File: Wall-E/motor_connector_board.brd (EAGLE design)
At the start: 104.1 x 41.9 mm, 19 parts, among them U1 JST_SH_4, U2 JST_SH_6, U3 JST_SH_6, U4 MOLEX_ULTRAFIT, U5 SMC

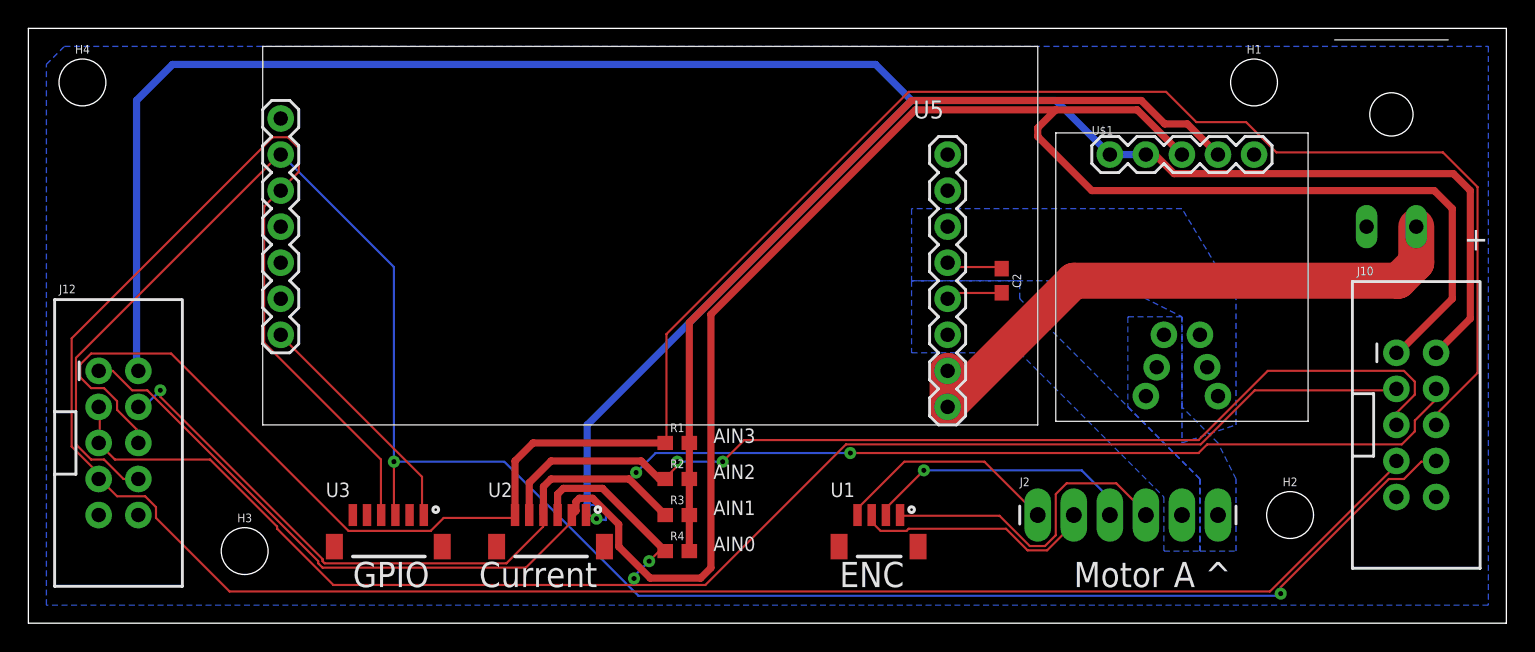
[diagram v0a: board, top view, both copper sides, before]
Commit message: completed first motor pcb
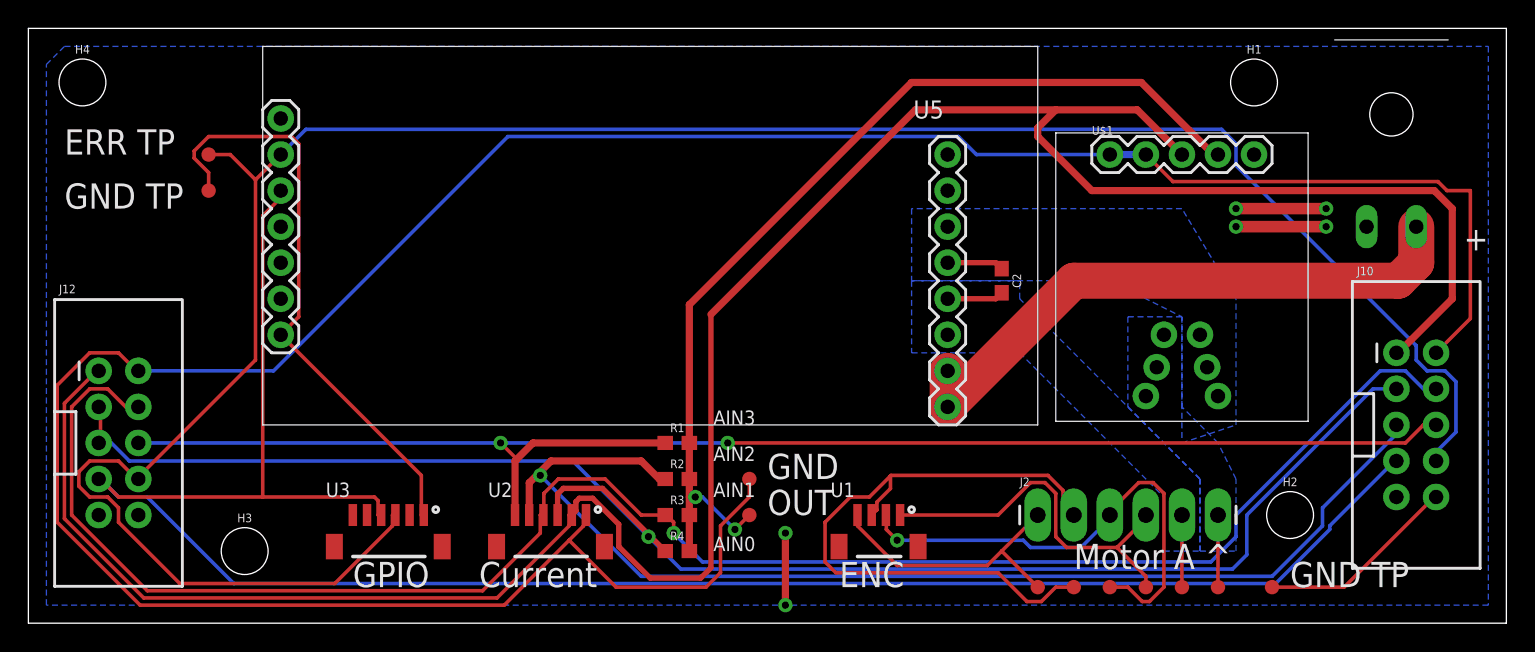
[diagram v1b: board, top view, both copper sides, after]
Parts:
- added TP1, TP10, TP11, TP2, TP3, TP4, TP5, TP6, TP7, TP8, TP9: TEST-POINT3X4, SparkFun-Connectors:PAD.03X.04
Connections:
- net ACS_GND: now also TP4.P$1
- net ACS_OUT: now also TP5.P$1
- net ENC_A: now also TP6.P$1
- net ENC_B: now also TP7.P$1
- net ENC_GND: now also TP9.P$1
- net ENC_VCC: now also TP8.P$1
- net GND: now also TP1.P$1, TP2.P$1
- net MOTORA: now also TP10.P$1
- net MOTORB: now also TP11.P$1
- net SMC_ERR: now also TP3.P$1
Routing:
- net GND: track 16.9 -> 74.1 mm, vias 0 -> 6
- net AIN3: track 152.0 -> 108.5 mm, vias 0 -> 2
- net ENC_A: track 17.1 -> 45.8 mm
- net SMC_ERR: track 142.2 -> 164.0 mm, vias 2 -> 0
- net ACS_GND: track 172.5 -> 194.2 mm, vias 1 -> 0
- net SMC_RST: track 162.4 -> 141.9 mm
- net AIN1: track 108.6 -> 126.5 mm, vias 3 -> 1
- net ENC_VCC: track 19.3 -> 34.9 mm
- net ACS_VCC: track 159.1 -> 170.5 mm
- net AIN2: track 73.1 -> 82.1 mm, vias 2 -> 1
- net ACS_OUT: track 61.4 -> 68.8 mm, vias 0 -> 2
- net MOTORA: track 0.00 -> 5.08 mm
- net MOTORB: track 4.05 -> 9.06 mm
- net ENC_GND: track 22.8 -> 26.7 mm
- net ENC_B: track 16.1 -> 19.7 mm
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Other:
- board text added: "ERR TP"
- board text added: "GND"
- board text added: "GND TP"
- board text added: "OUT"

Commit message: fixed error on ribbon cable connector
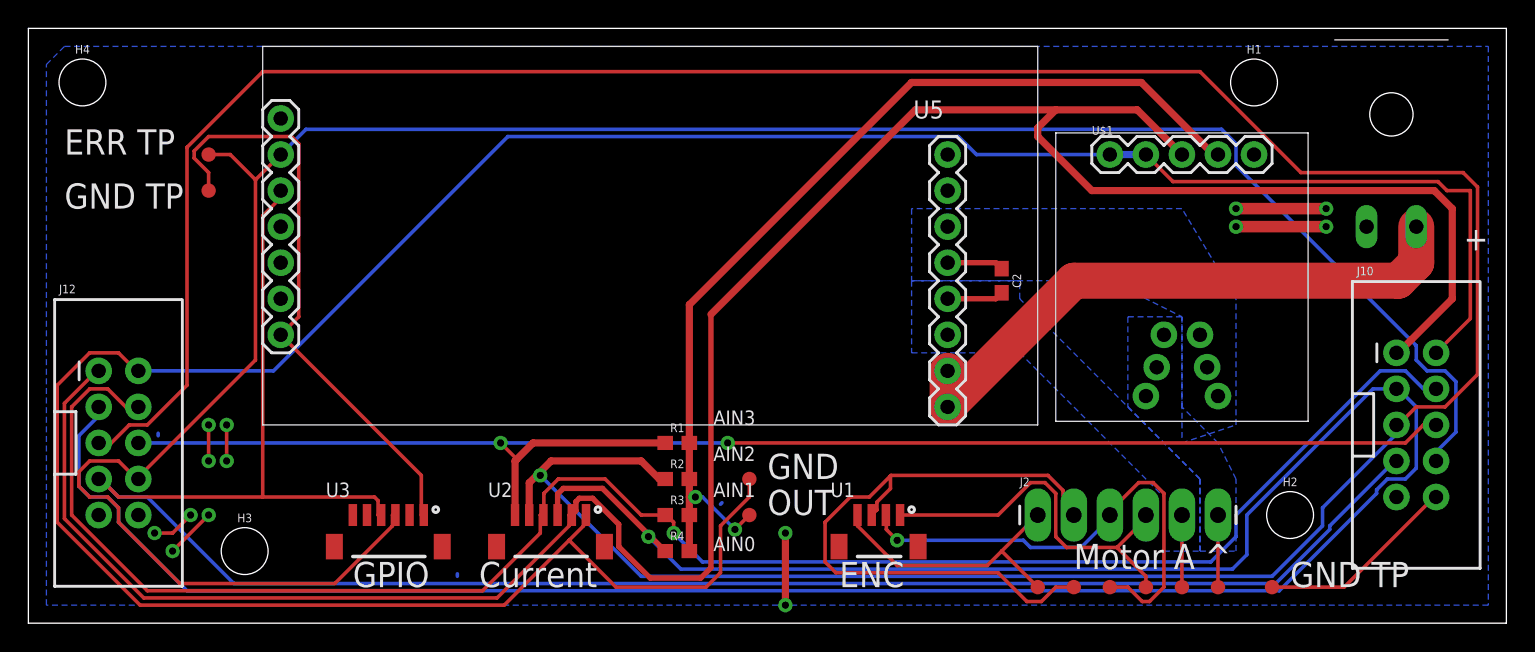
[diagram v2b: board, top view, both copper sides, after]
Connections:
- net AIN0: no longer J12.5
- net AIN2: now also J12.5
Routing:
- net AIN2: track 82.1 -> 223.6 mm
- net AIN0: track 116.0 -> 185.9 mm
- net GND: track 74.1 -> 86.4 mm, vias 6 -> 14
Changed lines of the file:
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@@
 <layer number="43" name="vRestrict" color="2" fill="10" visible="no" active="yes"/>
 <layer number="44" name="Drills" color="7" fill="1" visible="no" active="yes"/>
-<layer number="45" name="Holes" color="7" fill="1" visible="no" active="yes"/>
+<layer number="45" name="Holes" color="7" fill="1" visible="yes" active="yes"/>
 <layer number="46" name="Milling" color="3" fill="1" visible="no" active="yes"/>
 <layer number="47" name="Measures" color="7" fill="1" visible="no" active="yes"/>
@@
 <layer number="49" name="Reference" color="7" fill="1" visible="no" active="yes"/>
 <layer number="50" name="dxf" color="7" fill="1" visible="no" active="no"/>
-<layer number="51" name="tDocu" color="6" fill="1" visible="no" active="yes"/>
+<layer number="51" name="tDocu" color="6" fill="1" visible="yes" active="yes"/>
 <layer number="52" name="bDocu" color="7" fill="1" visible="no" active="yes"/>
 <layer number="53" name="tGND_GNDA" color="7" fill="9" visible="no" active="no"/>
@@
 <wire x1="114.3" y1="0" x2="119.38" y2="0" width="0.254" layer="1"/>
 <wire x1="119.38" y1="0" x2="125.73" y2="6.35" width="0.254" layer="1"/>
+<wire x1="56.896" y1="0.762" x2="56.896" y2="0.939796875" width="0.254" layer="16"/>
+<wire x1="35.814" y1="10.668" x2="35.814" y2="10.845796875" width="0.254" layer="16"/>
+<wire x1="75.438" y1="5.842" x2="75.54193125" y2="5.94593125" width="0.254" layer="16"/>
+<via x="38.1" y="5.08" extent="1-16" drill="0.508"/>
+<via x="39.37" y="5.08" extent="1-16" drill="0.508"/>
+<via x="35.56" y="3.81" extent="1-16" drill="0.508"/>
+<via x="36.83" y="2.54" extent="1-16" drill="0.508"/>
+<via x="39.37" y="8.89" extent="1-16" drill="0.508"/>
+<via x="40.64" y="8.89" extent="1-16" drill="0.508"/>
+<via x="39.37" y="11.43" extent="1-16" drill="0.508"/>
+<via x="40.64" y="11.43" extent="1-16" drill="0.508"/>
+<wire x1="39.37" y1="11.43" x2="39.37" y2="8.89" width="0.254" layer="1"/>
+<wire x1="40.64" y1="11.43" x2="40.64" y2="8.89" width="0.254" layer="1"/>
+<wire x1="38.1" y1="5.08" x2="36.83" y2="3.81" width="0.254" layer="1"/>
+<wire x1="36.83" y1="3.81" x2="35.56" y2="3.81" width="0.254" layer="1"/>
+<wire x1="39.37" y1="5.08" x2="36.83" y2="2.54" width="0.254" layer="1"/>
 </signal>
 <signal name="MOTORA">
@@
 <wire x1="62.738" y1="7.874" x2="62.611" y2="8.001" width="0.254" layer="1"/>
 <via x="62.738" y="7.874" extent="1-16" drill="0.508"/>
+<contactref element="J12" pad="5"/>
+<wire x1="32.512" y1="10.16" x2="31.623" y2="10.16" width="0.254" layer="1"/>
+<wire x1="33.782" y1="11.43" x2="32.512" y2="10.16" width="0.254" layer="1"/>
+<wire x1="35.052" y1="11.43" x2="33.782" y2="11.43" width="0.254" layer="1"/>
+<wire x1="37.846" y1="14.224" x2="35.052" y2="11.43" width="0.254" layer="1"/>
+<wire x1="37.846" y1="30.988" x2="37.846" y2="14.224" width="0.254" layer="1"/>
+<wire x1="43.18" y1="36.322" x2="37.846" y2="30.988" width="0.254" layer="1"/>
+<wire x1="109.22" y1="36.322" x2="43.18" y2="36.322" width="0.254" layer="1"/>
+<wire x1="116.332" y1="29.21" x2="109.22" y2="36.322" width="0.254" layer="1"/>
+<wire x1="127.762" y1="29.21" x2="116.332" y2="29.21" width="0.254" layer="1"/>
+<wire x1="128.778" y1="28.194" x2="127.762" y2="29.21" width="0.254" layer="1"/>
+<wire x1="128.778" y1="14.986" x2="128.778" y2="28.194" width="0.254" layer="1"/>
+<wire x1="126.492" y1="12.7" x2="128.778" y2="14.986" width="0.254" layer="1"/>
+<wire x1="124.46" y1="12.7" x2="126.492" y2="12.7" width="0.254" layer="1"/>
+<wire x1="123.19" y1="11.43" x2="124.46" y2="12.7" width="0.254" layer="1"/>
+<wire x1="123.19" y1="11.43" x2="123.063" y2="11.43" width="0.254" layer="1"/>
 </signal>
 <signal name="AIN1">
@@
 <contactref element="J10" pad="3"/>
 <contactref element="J12" pad="3"/>
-<contactref element="J12" pad="5"/>
 <wire x1="71.54" y1="2.54" x2="70.441" y2="3.639" width="0.381" layer="1"/>
 <wire x1="70.441" y1="3.639" x2="67.1204" y2="6.9596" width="0.381" layer="1"/>
@@
 <wire x1="67.1204" y1="6.9596" x2="64.3636" y2="6.9596" width="0.381" layer="1"/>
 <wire x1="64.3636" y1="6.9596" x2="63.96" y2="6.556" width="0.381" layer="1"/>
-<wire x1="31.75" y1="12.7" x2="31.75" y2="10.16" width="0.254" layer="1"/>
-<wire x1="31.75" y1="10.16" x2="31.623" y2="10.16" width="0.254" layer="1"/>
 <wire x1="31.75" y1="12.7" x2="31.623" y2="12.7" width="0.254" layer="1"/>
 <wire x1="121.412" y1="13.97" x2="123.063" y2="13.97" width="0.254" layer="16"/>
@@
 <wire x1="70.358" y1="3.556" x2="72.644" y2="1.27" width="0.254" layer="16"/>
 <wire x1="70.358" y1="3.556" x2="70.441" y2="3.639" width="0.254" layer="1"/>
-<wire x1="32.512" y1="10.16" x2="31.623" y2="10.16" width="0.254" layer="16"/>
-<wire x1="33.782" y1="8.89" x2="32.512" y2="10.16" width="0.254" layer="16"/>
-<wire x1="65.024" y1="8.89" x2="33.782" y2="8.89" width="0.254" layer="16"/>
-<wire x1="70.358" y1="3.556" x2="65.024" y2="8.89" width="0.254" layer="16"/>
 <via x="70.358" y="3.556" extent="1-16" drill="0.508"/>
+<wire x1="31.496" y1="11.938" x2="31.496" y2="12.7" width="0.254" layer="16"/>
+<wire x1="30.226" y1="10.668" x2="31.496" y2="11.938" width="0.254" layer="16"/>
+<wire x1="30.226" y1="7.112" x2="30.226" y2="10.668" width="0.254" layer="16"/>
+<wire x1="30.988" y1="6.35" x2="30.226" y2="7.112" width="0.254" layer="16"/>
+<wire x1="32.258" y1="6.35" x2="30.988" y2="6.35" width="0.254" layer="16"/>
+<wire x1="33.02" y1="5.588" x2="32.258" y2="6.35" width="0.254" layer="16"/>
+<wire x1="33.02" y1="4.572" x2="33.02" y2="5.588" width="0.254" layer="16"/>
+<wire x1="37.846" y1="-0.254" x2="33.02" y2="4.572" width="0.254" layer="16"/>
+<wire x1="114.808" y1="-0.254" x2="37.846" y2="-0.254" width="0.254" layer="16"/>
+<wire x1="121.666" y1="6.604" x2="114.808" y2="-0.254" width="0.254" layer="16"/>
+<wire x1="121.666" y1="6.858" x2="121.666" y2="6.604" width="0.254" layer="16"/>
+<wire x1="122.428" y1="7.62" x2="121.666" y2="6.858" width="0.254" layer="16"/>
+<wire x1="123.698" y1="7.62" x2="122.428" y2="7.62" width="0.254" layer="16"/>
+<wire x1="124.46" y1="8.382" x2="123.698" y2="7.62" width="0.254" layer="16"/>
+<wire x1="124.46" y1="12.7" x2="124.46" y2="8.382" width="0.254" layer="16"/>
+<wire x1="123.19" y1="13.97" x2="124.46" y2="12.7" width="0.254" layer="16"/>
+<wire x1="31.496" y1="12.7" x2="31.623" y2="12.7" width="0.254" layer="16"/>
+<wire x1="123.19" y1="13.97" x2="123.063" y2="13.97" width="0.254" layer="16"/>
 </signal>
 <signal name="SMC_ERR">

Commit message: added voltage divider for current sense, rerouted current sense power to a 3.3 line, and minor tweaks to routing
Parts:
- added R5, R6: 10k, SparkFun-Resistors:0603
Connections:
- new net ACS_3.3OUT: R5.2, U$1.4
- net ACS_OUT: now also R5.1, R6.2; no longer U$1.4
- net ACS_VCC: now also U3.2; no longer U2.2
- net GND: now also R6.1
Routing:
- net ACS_3.3OUT: track 0.00 -> 49.2 mm
- net ACS_OUT: track 68.8 -> 22.7 mm
- net AIN2: track 223.6 -> 250.1 mm, vias 1 -> 2
- net GND: track 86.4 -> 67.1 mm, vias 14 -> 18
- net SMC_ERR: track 164.0 -> 183.2 mm, vias 0 -> 1
- net ACS_VCC: track 170.5 -> 160.9 mm, vias 0 -> 3
- net SMC_RST: track 141.9 -> 147.7 mm
- added copper zone on layer 1, net GND
